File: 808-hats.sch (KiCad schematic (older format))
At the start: 40 parts, among them Q1 BC546, Q10 BC546, Q2 BC546, Q3 BC556, Q4 BC556, Q5 BC546, Q6 BC546, Q7 BC546, Q8 BC546, Q9 BC546

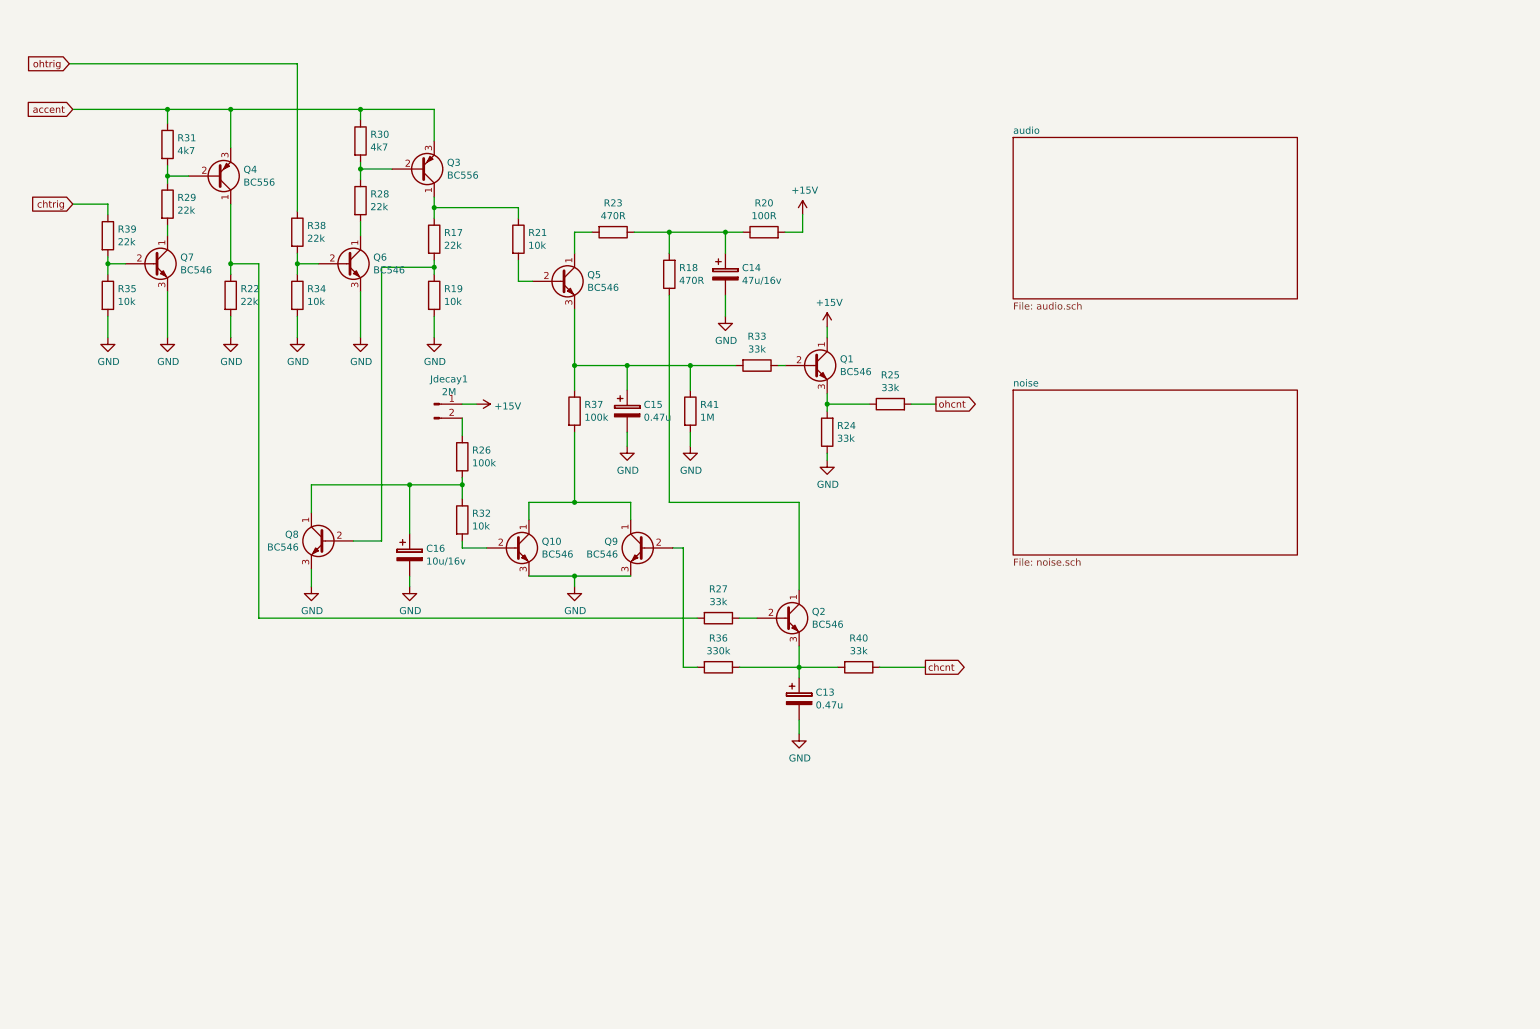
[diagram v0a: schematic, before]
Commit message: added trigger conditioning and accent pullup
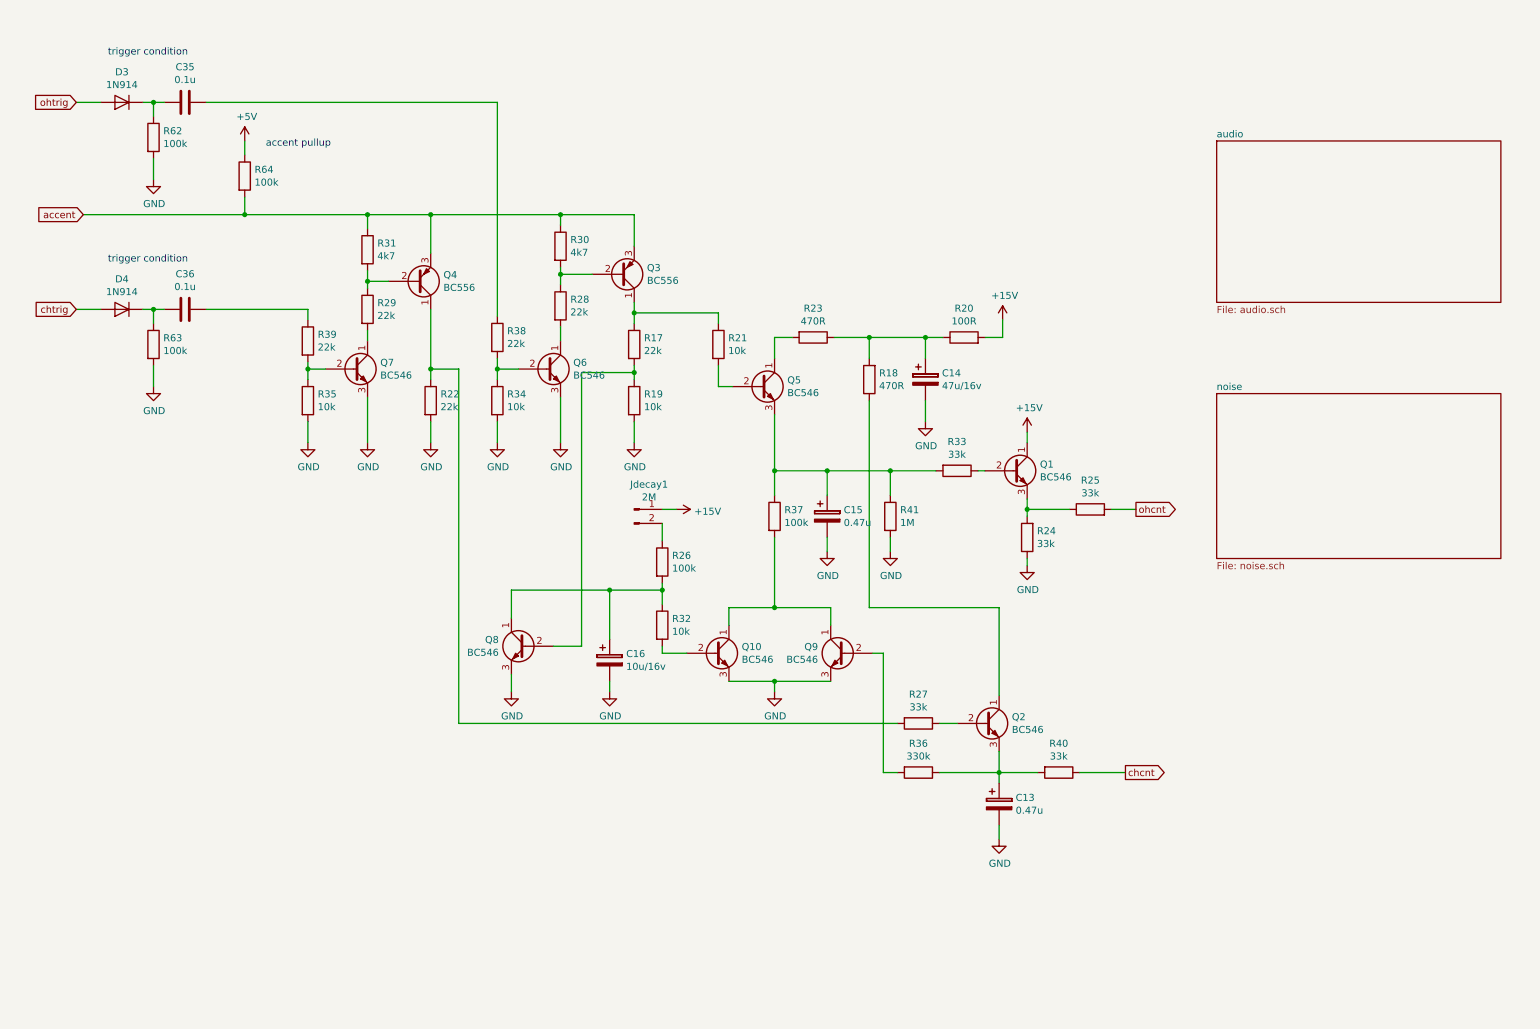
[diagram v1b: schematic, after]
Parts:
- added C35, C36: 0.1u, symbol Device:C
- added D3, D4: 1N914, Diode_THT:D_DO-35_SOD27_P7.62mm_Horizontal, symbol Diode:1N914
- added R62, R63, R64: 100k, symbol Device:R
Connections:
- net GND: now also R62.2, R63.2
- net accent: now also R64.2
- net chtrig: now also D4.2 (A); no longer R39.1
- net ohtrig: now also D3.2 (A); no longer R38.1
- new net: C35.1, R38.1
- new net: C36.1, R39.1
- new net: C36.2, D4.1 (K), R63.1
- new net: C35.2, D3.1 (K), R62.1
- new net +5V: R64.1
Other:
- note added: "accent pullup"
- note added: "trigger condition"
- moved on the sheet: C13, C14, C15, C16, Jdecay1, Q1, Q10, Q2, Q3, Q4, Q5, Q6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

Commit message: added power
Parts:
- added C37, C38: 10u/25v, Capacitor_SMD:C_0805_2012Metric_Pad1.33x1.40mm_HandSolder, symbol Device:C
- added J5: trig/accent, symbol Connector:Conn_01x03_Male
- added L1, L2: BEAD, Inductor_SMD:L_0603_1608Metric_Pad1.05x0.95mm_HandSolder, symbol Device:Ferrite_Bead_Small
- added P1: MTA-156-4, mta-156:MTA-156-4, symbol mta-156:MTA-156-4
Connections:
- net +15V: now also C37.1, L2.1
- net GND: now also C37.2, C38.1, P1.2 (P2), P1.3 (P3)
- net accent: now also J5.3 (Pin_3)
- net chtrig: now also J5.2 (Pin_2)
- net ohtrig: now also J5.1 (Pin_1)
- new net: L2.2, P1.1 (P1)
- new net: L1.2, P1.4 (P4)
- new net -15V: C38.2, L1.1
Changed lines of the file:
@@
 EESchema Schematic File Version 4
 LIBS:808-hats-cache
+LIBS:shift-triggers-cache
+LIBS:mod-dac-cache
 EELAYER 26 0
 EELAYER END
@@
 Text Notes 2150 1425 0    50   ~ 0
 accent pullup
+$Comp
+L Connector:Conn_01x03_Male J5
+U 1 1 5CB287CA
+P 975 6200
+F 0 "J5" H 1081 6478 50  0000 C CNN
+F 1 "trig/accent" H 1081 6387 50  0000 C CNN
+F 2 "" H 975 6200 50  0001 C CNN
+F 3 "~" H 975 6200 50  0001 C CNN
+	1    975  6200
+	1    0    0    -1
+$EndComp
+Text GLabel 1300 6100 2    50   Output ~ 0
+ohtrig
+Text GLabel 1300 6200 2    50   Output ~ 0
+chtrig
+Text GLabel 1300 6300 2    50   Output ~ 0
+accent
+Wire Wire Line
+	1175 6100 1300 6100
+Wire Wire Line
+	1300 6200 1175 6200
+Wire Wire Line
+	1175 6300 1300 6300
+Wire Wire Line
+	3300 6525 3700 6525
+Wire Wire Line
+	3700 6525 3700 6600
+Wire Wire Line
+	3700 6625 3300 6625
+Wire Wire Line
+	3500 6725 3300 6725
+$Comp
+L power:+15V #PWR07
+U 1 1 5CB41248
+P 4325 6200
+F 0 "#PWR07" H 4325 6050 50  0001 C CNN
+F 1 "+15V" H 4340 6373 50  0000 C CNN
+F 2 "" H 4325 6200 50  0001 C CNN
+F 3 "" H 4325 6200 50  0001 C CNN
+	1    4325 6200
+	1    0    0    -1
+$EndComp
+$Comp
+L power:-15V #PWR06
+U 1 1 5CB4124E
+P 4000 7400
+F 0 "#PWR06" H 4000 7500 50  0001 C CNN
+F 1 "-15V" H 4015 7573 50  0000 C CNN
+F 2 "" H 4000 7400 50  0001 C CNN
+F 3 "" H 4000 7400 50  0001 C CNN
+	1    4000 7400
+	-1   0    0    1
+$EndComp
+$Comp
+L Device:Ferrite_Bead_Small L2
+U 1 1 5CB41254
+P 3825 6425
+F 0 "L2" V 3588 6425 50  0000 C CNN
+F 1 "BEAD" V 3679 6425 50  0000 C CNN
+F 2 "Inductor_SMD:L_0603_1608Metric_Pad1.05x0.95mm_HandSolder" V 3755 6425 50  0001 C CNN
+F 3 "~" H 3825 6425 50  0001 C CNN
+	1    3825 6425
+	0    1    1    0
+$EndComp
+$Comp
+L Device:Ferrite_Bead_Small L1
+U 1 1 5CB4125B
+P 3600 7150
+F 0 "L1" V 3363 7150 50  0000 C CNN
+F 1 "BEAD" V 3454 7150 50  0000 C CNN
+F 2 "Inductor_SMD:L_0603_1608Metric_Pad1.05x0.95mm_HandSolder" V 3530 7150 50  0001 C CNN
+F 3 "~" H 3600 7150 50  0001 C CNN
+	1    3600 7150
+	0    1    1    0
+$EndComp
+$Comp
+L mta-156:MTA-156-4 P1
+U 1 1 5CB41262
+P 3100 6575
+F 0 "P1" H 3019 6940 50  0000 C CNN
+F 1 "MTA-156-4" H 3019 6849 50  0000 C CNN
+F 2 "mta-156:MTA-156-4" H 3100 6575 50  0001 C CNN
+F 3 "" H 3100 6575 50  0000 C CNN
+	1    3100 6575
+	-1   0    0    -1
+$EndComp
+Wire Wire Line
+	3700 7150 4000 7150
+Wire Wire Line
+	4000 7150 4000 7400
+Connection ~ 4000 7150
+$Comp
+L power:GND #PWR05
+U 1 1 5CB4126C
+P 3800 6600
+F 0 "#PWR05" H 3800 6350 50  0001 C CNN
+F 1 "GND" H 3805 6427 50  0000 C CNN
+F 2 "" H 3800 6600 50  0001 C CNN
+F 3 "" H 3800 6600 50  0001 C CNN
+	1    3800 6600
+	1    0    0    -1
+$EndComp
+Wire Wire Line
+	3800 6600 3700 6600
+Connection ~ 3700 6600
+Wire Wire Line
+	3700 6600 3700 6625
+$Comp
+L power:GND #PWR?
+U 1 1 5CB41275
+P 5075 6775
+AR Path="/5CB3E34A/5CB41275" Ref="#PWR?"  Part="1"
+AR Path="/5CB41275" Ref="#PWR08"  Part="1"
+F 0 "#PWR08" H 5075 6525 50  0001 C CNN
+F 1 "GND" H 5080 6602 50  0000 C CNN
+F 2 "" H 5075 6775 50  0001 C CNN
+F 3 "" H 5075 6775 50  0001 C CNN
+	1    5075 6775
+	0    -1   -1   0
+$EndComp
+Wire Wire Line
+	3500 6725 3500 7150
+$Comp
+L power:PWR_FLAG #FLG03
+U 1 1 5CB4127C
+P 4725 7275
+F 0 "#FLG03" H 4725 7350 50  0001 C CNN
+F 1 "PWR_FLAG" H 4725 7449 50  0000 C CNN
+F 2 "" H 4725 7275 50  0001 C CNN
+F 3 "~" H 4725 7275 50  0001 C CNN
+	1    4725 7275
+	-1   0    0    1
+$EndComp
+$Comp
+L power:PWR_FLAG #FLG02
+U 1 1 5CB41282
+P 4700 6325
+F 0 "#FLG02" H 4700 6400 50  0001 C CNN
+F 1 "PWR_FLAG" H 4700 6499 50  0000 C CNN
+F 2 "" H 4700 6325 50  0001 C CNN
+F 3 "~" H 4700 6325 50  0001 C CNN
+	1    4700 6325
+	1    0    0    -1
+$EndComp
+$Comp
+L power:PWR_FLAG #FLG01
+U 1 1 5CB41288
+P 3850 6525
+F 0 "#FLG01" H 3850 6600 50  0001 C CNN
+F 1 "PWR_FLAG" V 3850 6653 50  0000 L CNN
+F 2 "" H 3850 6525 50  0001 C CNN
+F 3 "~" H 3850 6525 50  0001 C CNN
+	1    3850 6525
+	0    1    1    0
+$EndComp
+Wire Wire Line
+	3850 6525 3700 6525
+Connection ~ 3700 6525
+Wire Wire Line
+	4500 7100 4500 7150
+Wire Wire Line
+	4500 7150 4725 7150
+Connection ~ 4500 7150
+Wire Wire Line
+	4500 6750 4500 6775
+Connection ~ 4500 6775
+Wire Wire Line
+	4500 6775 4500 6800
+Wire Wire Line
+	4000 7150 4500 7150
+Wire Wire Line
+	3925 6425 4325 6425
+Wire Wire Line
+	4700 6325 4700 6425
+Wire Wire Line
+	4500 6450 4500 6425
+Connection ~ 4500 6425
+Wire Wire Line
+	4500 6425 4700 6425
+Wire Wire Line
+	4325 6425 4325 6200
+Connection ~ 4325 6425
+Wire Wire Line
+	4325 6425 4500 6425
+Wire Wire Line
+	4725 7275 4725 7150
+$Comp
+L Device:C C?
+U 1 1 5CB412A0
+P 4500 6600
+AR Path="/5CB3E34A/5CB412A0" Ref="C?"  Part="1"
+AR Path="/5CB412A0" Ref="C37"  Part="1"
+F 0 "C37" H 4615 6646 50  0000 L CNN
+F 1 "10u/25v" H 4615 6555 50  0000 L CNN
+F 2 "Capacitor_SMD:C_0805_2012Metric_Pad1.33x1.40mm_HandSolder" H 4538 6450 50  0001 C CNN
+F 3 "~" H 4500 6600 50  0001 C CNN
+	1    4500 6600
+	1    0    0    -1
+$EndComp
+$Comp
+L Device:C C?
+U 1 1 5CB412A7
+P 4500 6950
+AR Path="/5CB3E34A/5CB412A7" Ref="C?"  Part="1"
+AR Path="/5CB412A7" Ref="C38"  Part="1"
+F 0 "C38" H 4615 6996 50  0000 L CNN
+F 1 "10u/25v" H 4615 6905 50  0000 L CNN
+F 2 "Capacitor_SMD:C_0805_2012Metric_Pad1.33x1.40mm_HandSolder" H 4538 6800 50  0001 C CNN
+F 3 "~" H 4500 6950 50  0001 C CNN
+	1    4500 6950
+	1    0    0    -1
+$EndComp
+Wire Wire Line
+	4500 6775 5075 6775
+Wire Wire Line
+	3300 6425 3725 6425
 $EndSCHEMATC

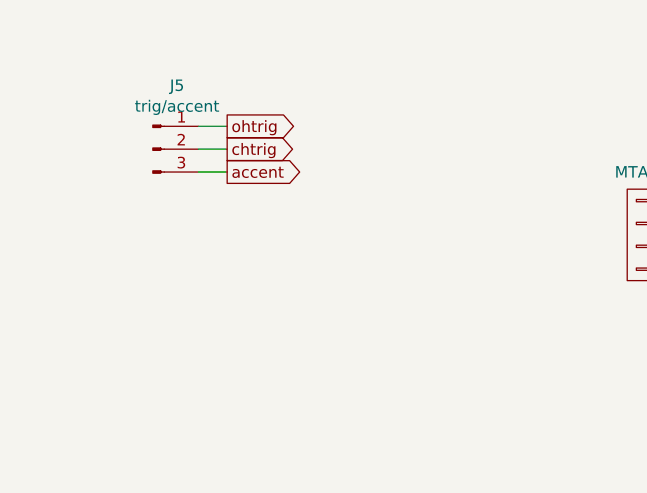
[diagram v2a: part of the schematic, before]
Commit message: fixup noise generator connections
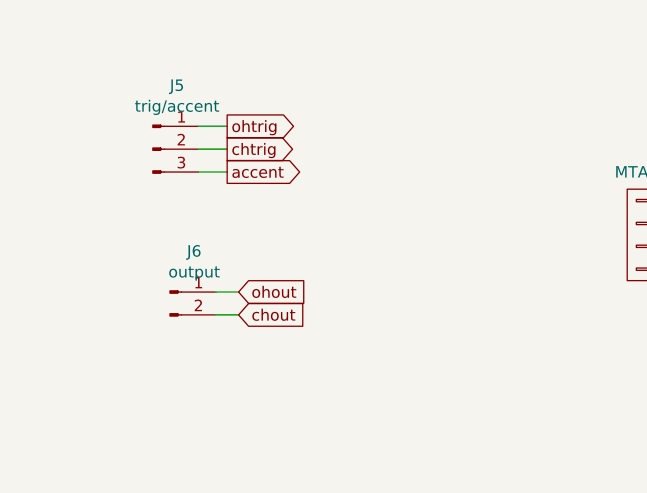
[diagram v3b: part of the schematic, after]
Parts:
- added J6: output, symbol Connector:Conn_01x02_Male
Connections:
- new net chout: J6.2 (Pin_2)
- new net ohout: J6.1 (Pin_1)
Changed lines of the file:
@@
 EESchema Schematic File Version 4
 LIBS:808-hats-cache
-LIBS:shift-triggers-cache
-LIBS:mod-dac-cache
 EELAYER 26 0
 EELAYER END
@@
 Wire Wire Line
 	3300 6425 3725 6425
+$Comp
+L Connector:Conn_01x02_Male J6
+U 1 1 5CB6481D
+P 1050 6825
+F 0 "J6" H 1156 7003 50  0000 C CNN
+F 1 "output" H 1156 6912 50  0000 C CNN
+F 2 "" H 1050 6825 50  0001 C CNN
+F 3 "~" H 1050 6825 50  0001 C CNN
+	1    1050 6825
+	1    0    0    -1
+$EndComp
+Text GLabel 1350 6925 2    50   Input ~ 0
+chout
+Text GLabel 1350 6825 2    50   Input ~ 0
+ohout
+Wire Wire Line
+	1350 6825 1250 6825
+Wire Wire Line
+	1250 6925 1350 6925
 $EndSCHEMATC
